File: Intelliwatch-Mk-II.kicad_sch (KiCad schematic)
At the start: 75 parts, among them J1 Voltmeter Probes, J2 DC Power Input, J3 USB_C_Receptacle_USB2.0_16P, J4 Flashlight Terminals, J5 CONN LCD 1.8 TFT SPI, J6 Conn 7S-4D HW-069 I2C, Q1 NDS331N, SW1 PWR SPST, SW2 EN Button, SW3 LCD LED SPST, SW4 Cherry MX Keyswitch, SW5 Cherry MX Keyswitch, SW6 Cherry MX Keyswitch, SW7 Cherry MX Keyswitch, SW8 PROG Button, U1 SN74HC02N, U2 MCP3421A0T-ECH, U3 74AHC1G04GW_125, U4 74AHC1G04GW_125, U5 LM7805, U6 CH340C, U7 SY8120IABC, U8 QMC5883L, U9 ESP32-WROOM-32UE

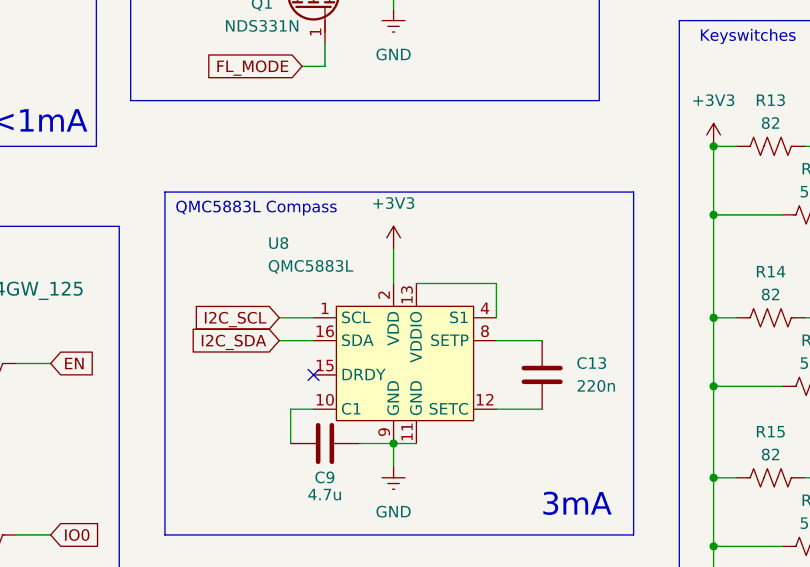
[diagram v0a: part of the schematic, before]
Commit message: ADDED TFT LCD footprint w/clearance. FIXED trace width and clearance. TODO arrange PCB.
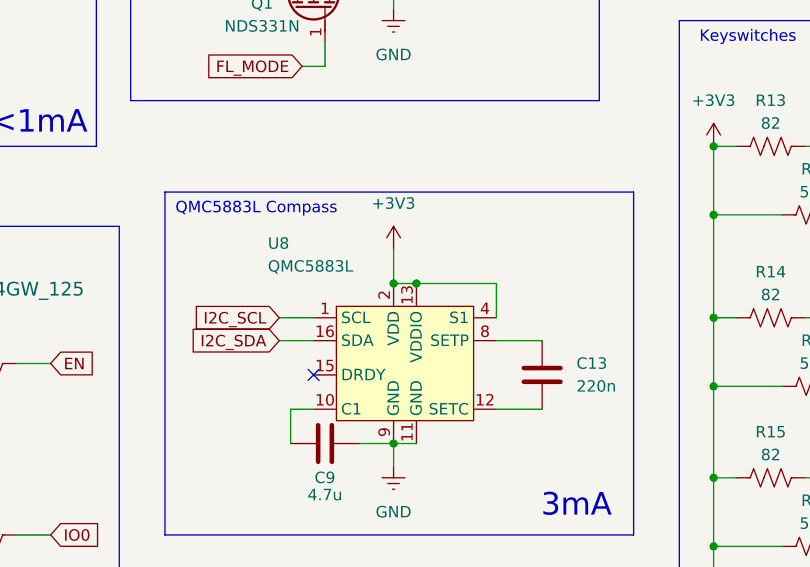
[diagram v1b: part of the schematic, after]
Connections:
- net +3V3: now also U8.13 (VDDIO), U8.4 (S1)
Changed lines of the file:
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@@
+	)
+	(junction
+		(at 133.35 203.2)
+		(diameter 0)
+		(color 0 0 0 0)
 	)
 	(junction
@@
 	(junction
 		(at 182.88 88.9)
+		(diameter 0)
+		(color 0 0 0 0)
+	)
+	(junction
+		(at 130.81 203.2)
 		(diameter 0)
 		(color 0 0 0 0)
@@
 		)
 		(stroke
+			(width 0)
+			(type default)
+		)
+	)
+	(wire
+		(pts
+			(xy 130.81 203.2) (xy 133.35 203.2)
+		)
+		(stroke

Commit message: FIXED board dimensions to be within minimum to avoid engineering fee. ADDED traces and copper areas for all power/ground nets. TODO is connecting signal lines, and maybe try using that autorouter plugin.
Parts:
- U5: footprint PCM_Package_TO_SOT_THT_AKL:TO-220-3_Horizontal_TabDown -> PCM_Package_TO_SOT_THT_AKL:TO-220-3_Vertical
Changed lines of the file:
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@@
 			)
 		)
-		(property "Footprint" "PCM_Package_TO_SOT_THT_AKL:TO-220-3_Horizontal_TabDown"
+		(property "Footprint" "PCM_Package_TO_SOT_THT_AKL:TO-220-3_Vertical"
 			(at 77.47 57.15 0)
 			(effects

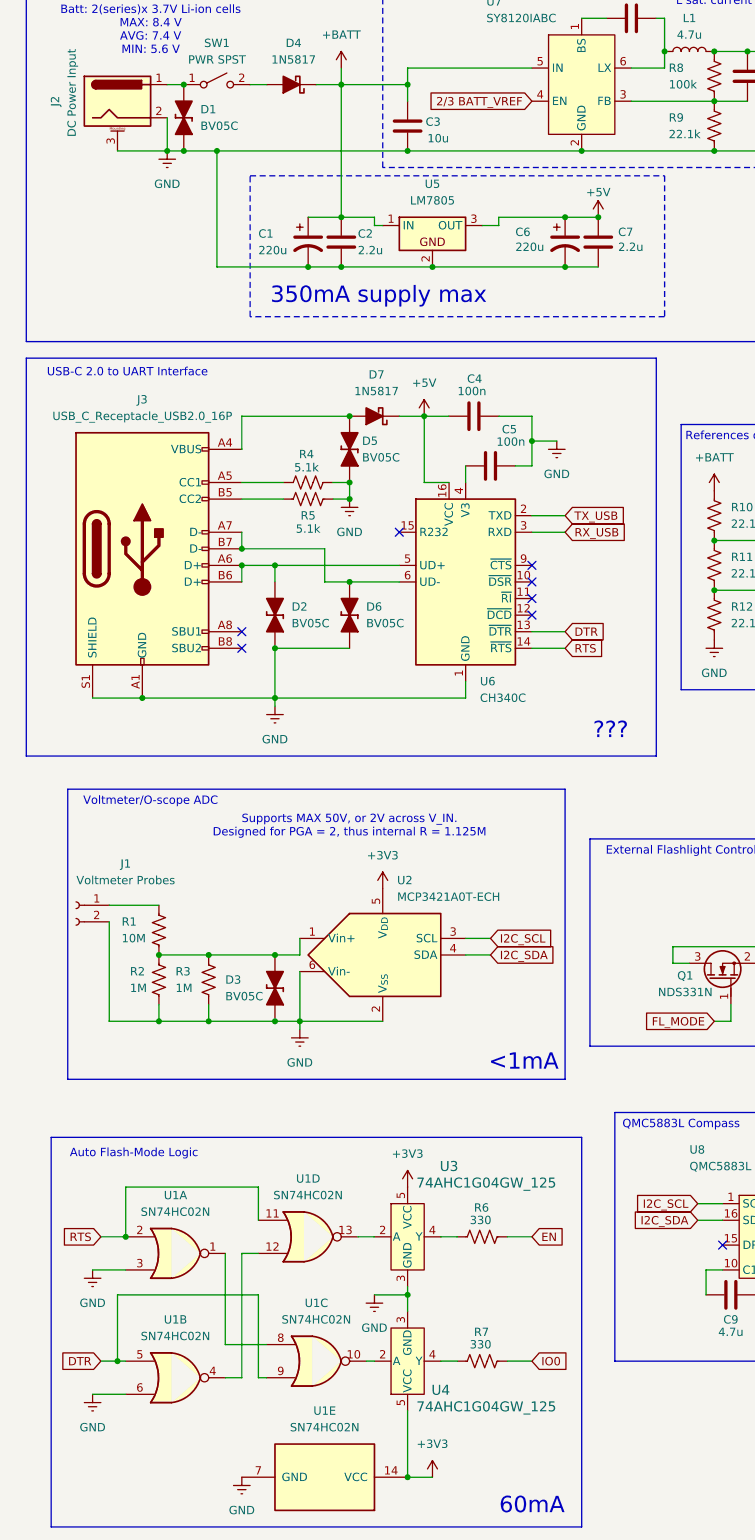
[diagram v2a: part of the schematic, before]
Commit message: FIXED ESD/TVS diodes to be a different part with practically identical specs.
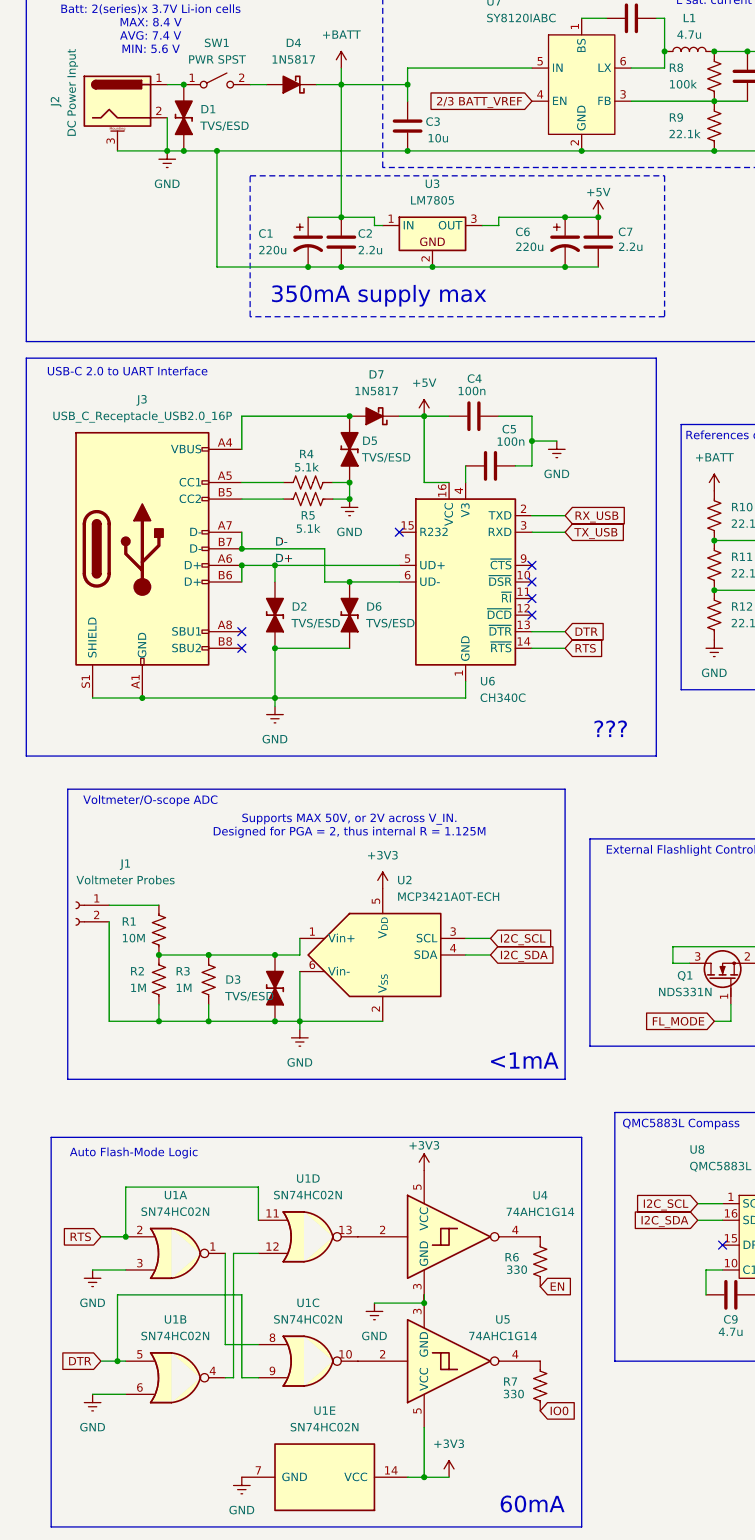
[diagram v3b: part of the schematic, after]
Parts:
- removed U3, U4: 74AHC1G04GW_125, Package_TO_SOT_SMD:SOT-353_SC-70-5, symbol 74AHC1G04GV,125:74AHC1G04GW_125
- added U4, U5: 74AHC1G14, PCM_Package_TO_SOT_SMD_AKL:SOT-353_SC-70-5_BigPads, symbol 74xGxx:74AHC1G14
- D1, D2, D3, D5, D6: value BV05C -> TVS/ESD; LCSC Part # C2841841 -> C5180217
- J2: LCSC Part # n/a -> C720557
- renumbered U5 to U3
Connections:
- net +3V3: now also U4.5 (VCC), U5.5 (VCC)
- net GND: now also U4.3 (GND), U5.3 (GND)
- net IO0: now also R7.2; no longer R7.1
- net RX_USB: now also U6.2 (TXD); no longer U6.3 (RXD)
- net TX_USB: now also U6.3 (RXD); no longer U6.2 (TXD)
- net D-: now reaches D6.1 (K), J3.A7 (D-), J3.B7 (D-), U6.6 (UD-)
- net D+: now reaches D2.1 (K), J3.A6 (D+), J3.B6 (D+), U6.5 (UD+)
- net at U1.10: now also U5.2
- net at U1.13: now also U4.2
- net at R6.2: now also U4.4
- new net: R7.1, U5.4
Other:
- moved on the sheet: R6, R7, U1C
